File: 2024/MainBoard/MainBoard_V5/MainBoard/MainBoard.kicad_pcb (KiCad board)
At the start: 2 copper layers, 115.8 x 60.5 mm, 90 parts, among them J1 Raspberry_Pi_2_3, J11 ADC2, J12 ADC2, J13 Drib, J14 UART, J15 TFT3, J16 CAN_CON, J2 fan, J3 USB_C_Receptacle_USB2.0_16P, J4 Conn_01x02_Pin, J5 MOLEX MINISPOX, J6 Debug, J7 ADC0, Q1 NMOS, Q2 PMOS, Q3 PMOS, SW1 SW_MEC_5E, SW2 Ras_1, SW3 Ras_2, SW4 SW_Wuerth_450301014042, U1 STM32F446RETx, U2 CH340E, U3 MOUDLE-SEEEDUINO-XIAO, U7 AZ1117-3.3, U8 MAX3051, Y1 CSTNE16M0V530000R0

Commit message: 途中経過（配置、電源線）
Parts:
- removed D12: 1N4148, Diode_SMD:D_SOD-123
- removed D9: LED, LED_SMD:LED_0603_1608Metric_Pad1.05x0.95mm_HandSolder
- removed H3, H6: MountingHole_Pad, MountingHole:MountingHole_3.2mm_M3_Pad_Via
- removed J11, J12: ADC2, Connector_JST:JST_PH_S3B-PH-K_1x03_P2.00mm_Horizontal
- removed J5: MOLEX MINISPOX, Connector_Molex:Molex_SPOX_5268-06A_1x06_P2.50mm_Horizontal
- removed J7: ADC0, Connector_JST:JST_PH_S3B-PH-K_1x03_P2.00mm_Horizontal
- removed Q3: PMOS, Package_TO_SOT_SMD:SOT-23
- removed R14: 1k, Resistor_SMD:R_0603_1608Metric_Pad0.98x0.95mm_HandSolder
- removed R23: 10K, Resistor_SMD:R_0603_1608Metric_Pad0.98x0.95mm_HandSolder
- removed R8, R9: 2.2k, Resistor_SMD:R_0603_1608Metric_Pad0.98x0.95mm_HandSolder
- removed U6: ~, Connector_PinHeader_2.54mm:PinHeader_1x04_P2.54mm_Vertical
- added C19: 330u, Capacitor_SMD:CP_Elec_8x11.9, B.Cu at (-38.6, 27.7)
- added C20: 330u, Capacitor_SMD:CP_Elec_8x11.9, B.Cu at (-26.6, 27.7)
- added C21: 330u, Capacitor_SMD:CP_Elec_8x11.9, B.Cu at (8.30, -14.9)
- added C22: 1u, Capacitor_SMD:C_0603_1608Metric_Pad1.08x0.95mm_HandSolder, B.Cu at (-30.1, 12.6)
- added C23: 330u, Capacitor_SMD:CP_Elec_8x11.9, F.Cu at (58.4, 17.4)
- added C24: 330u, Capacitor_SMD:CP_Elec_8x11.9, B.Cu at (-59.4, -25.5)
- added C25: 330u, Capacitor_SMD:CP_Elec_8x11.9, F.Cu at (47.8, 22.5)
- added C26: 1u, Capacitor_SMD:C_0603_1608Metric_Pad1.08x0.95mm_HandSolder, B.Cu at (-45.3, 30.0)
- added C27: 330u, Capacitor_SMD:CP_Elec_8x11.9, F.Cu at (17.1, 23.9)
- added D15: LED, LED_SMD:LED_0603_1608Metric_Pad1.05x0.95mm_HandSolder, F.Cu at (58.6, -15.6)
- added D16: SR54F, Diode_SMD:D_SMB_Handsoldering, F.Cu at (10.3, 15.5)
- added J8: MOLEX MINISPOX, Connector_Molex:Molex_SPOX_5268-05A_1x05_P2.50mm_Horizontal, B.Cu at (0.55, 22.1)
- added PS1: P783F-Q24-S6-S, MainBoard:CONV_P783F-Q24-S6-S, F.Cu at (23.5, 28.7)
- added Q4: Q_PMOS_GDS, Package_TO_SOT_SMD:TO-252-2, F.Cu at (37.0, 16.6)
- added R17: 1k, Resistor_SMD:R_0603_1608Metric_Pad0.98x0.95mm_HandSolder, F.Cu at (58.6, -12.1)
- added R21: 10k, Resistor_SMD:R_0603_1608Metric_Pad0.98x0.95mm_HandSolder, F.Cu at (27.4, 10.9)
- added U10: MPU9250, Connector_PinHeader_2.54mm:PinHeader_1x10_P2.54mm_Vertical, F.Cu at (-6.41, -11.2)
- added U9: LM39300R-5.0, MainBoard:LM39300, B.Cu at (-35.8, 17.3)
- J4: value Conn_01x02_Pin -> metor
- Q1: value NMOS -> DMMT5401; footprint MainBoard:SOT95P240X111-3N -> Package_TO_SOT_SMD:SOT-23-6
- Q2: value PMOS -> Q_NMOS_GSD; footprint Package_TO_SOT_SMD:SOT-23 -> Package_TO_SOT_SMD:SOT-23-3
- R22, R7: value 1k -> 10k
- moved J13 98.0 mm to (50.8, -24.6), turned to 0 degrees
- moved C12 90.8 mm to (-45.5, 29.2), turned to 90 degrees
- moved J14 79.3 mm to (39.8, -24.6), turned to 0 degrees
- moved J6 60.7 mm to (19.7, -28.8)
- moved U3 49.6 mm to (-24.8, 12.0), turned to 180 degrees
- moved D4 48.2 mm to (2.90, 34.6)
- moved D5 48.2 mm to (0.40, 34.6)
- moved Q2 46.7 mm to (40.8, -16.5)
- moved LS1 37.7 mm to (25.0, -19.4)
- moved R7 37.5 mm to (27.7, -11.3)
- moved D6 26.5 mm to (12.0, 35.0)
- moved R10 26.5 mm to (12.3, 39.3)
- moved R11 26.5 mm to (10.3, 39.3)
- moved C18 25.0 mm to (35.6, 11.8), turned to 180 degrees
- moved R22 19.2 mm to (27.4, 12.5), turned to 0 degrees
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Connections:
- C14 pad 1: +5VL -> Net-(D16-K)
- C18 pad 1: +5V -> VBUS
- C18 pad 2: Net-(Q2-G) -> GND
- LS1 pad N: Net-(Q1-D) -> Net-(Q2-D)
- Q1 pad 1: Net-(Q1-D) -> Net-(Q1A-C1)
- Q1 pad 2: Net-(D4-K) -> Net-(Q1A-B1)
- Q1 pad 3: GND -> Net-(Q1A-B1)
- Q2 pad 1: Net-(Q2-D) -> Net-(D4-K)
- Q2 pad 2: Net-(Q2-G) -> GND
- Q2 pad 3: +5V -> Net-(Q2-D)
- R22 pad 1: Net-(Q2-G) -> Net-(Q1A-C1)
- R22 pad 2: +5V -> GND
- R7 pad 2: Net-(Q1-D) -> Net-(Q2-D)
- U1 pad 33: unconnected-(U1-PB12-Pad33) -> SPI2.CS
- U1 pad 34: unconnected-(U1-PB13-Pad34) -> SPI2.CLK
- U1 pad 35: unconnected-(U1-PB14-Pad35) -> SPI2.MISO
- U1 pad 36: unconnected-(U1-PB15-Pad36) -> SPI2.MOSI
- U1 pad 46: unconnected-(U1-PA13-Pad46) -> SWDIO
- U1 pad 50: SWDIO -> unconnected-(U1-PA15-Pad50)
- U1 pad 58: I2C_SCL -> unconnected-(U1-PB6-Pad58)
- U1 pad 59: I2C_SDA -> unconnected-(U1-PB7-Pad59)
- U7 pad 3: +5VL -> Net-(D16-K)
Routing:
- net GND: track 616.9 -> 181.4 mm, vias 260 -> 1
- net +3.3V: track 334.1 -> 181.7 mm, vias 2 -> 0
- net +6V: track 0.00 -> 119.3 mm
- net LED_CS: track 105.5 -> 0.00 mm
- net MISO: track 111.2 -> 7.12 mm, vias 2 -> 0
- net NRST: track 95.6 -> 0.00 mm, vias 3 -> 0
- net ADC_SUB0: track 95.2 -> 0.00 mm, vias 3 -> 0
- net ADC_PHOTO1: track 94.2 -> 0.00 mm, vias 4 -> 0
- net SCK: track 110.3 -> 20.8 mm, vias 2 -> 0
- net MOSI: track 115.1 -> 30.2 mm, vias 2 -> 0
- net ADC_PHOTO0: track 84.8 -> 0.00 mm, vias 3 -> 0
- net Ras_TX: track 82.0 -> 0.00 mm, vias 3 -> 0
- net UART1_RX: track 81.3 -> 0.00 mm, vias 4 -> 0
- net UART1_TX: track 79.9 -> 0.00 mm, vias 4 -> 0
- net Ras_RX: track 78.8 -> 0.00 mm, vias 1 -> 0
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- removed copper zone on B.Cu, net GND
- removed copper zone on F.Cu, net GND
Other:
- board size 115.8 x 60.5 mm -> 130.5 x 65 mm
- board text removed: "0"
- board text removed: "1"
- board text removed: "10k"
- board text removed: "120"
- board text removed: "1k"
- board text removed: "2"
- board text removed: "2.2k"
- board text removed: "3.3V"
- board text removed: "4.7k"
- board text removed: "5V"
- board text removed: "ADC"
- board text removed: "BNO055"
- board text removed: "C"
- board text removed: "CAN"
- board text removed: "CANH"
- board text removed: "CANL"
- board text removed: "Designed by Riku Miyazaki"
- board text removed: "Drib"
- board text removed: "GND"
- board text removed: "H"
- board text removed: "Mainboard v.4"
- board text removed: "NMOS"
- board text removed: "NRST"
- board text removed: "Osc"
- board text removed: "PMOS"
- board text removed: "Photo0"
- board text removed: "Power"
- board text removed: "R"
- board text removed: "RX"
- board text removed: "Ras1"
- board text removed: "Ras2"
- board text removed: "Ri-one"
- board text removed: "STM32 F446RE"
- board text removed: "SWCLK"
- board text removed: "SWDIO"
- board text removed: "Sound"
- board text removed: "TX"
- board text removed: "TypeC"
- board text removed: "USB← →SWD"
- board text removed: "VD"
- board text removed: "Write"
- board text removed: "X"
- board text removed: "Xiao RP2040"
- board text removed: "photo1"
- board text removed: "←1 2→"

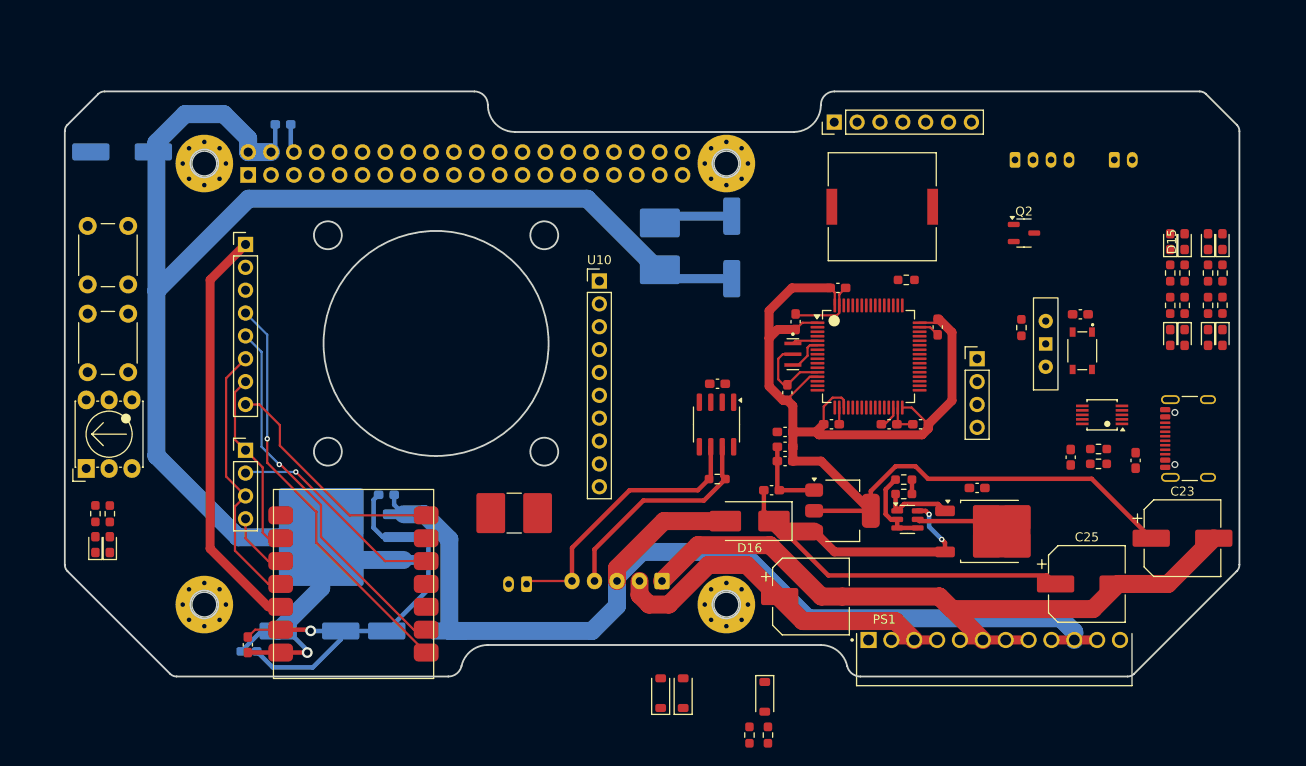
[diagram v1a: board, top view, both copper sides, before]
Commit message: アートワーク第一弾完成（ビア・シルク抜き）
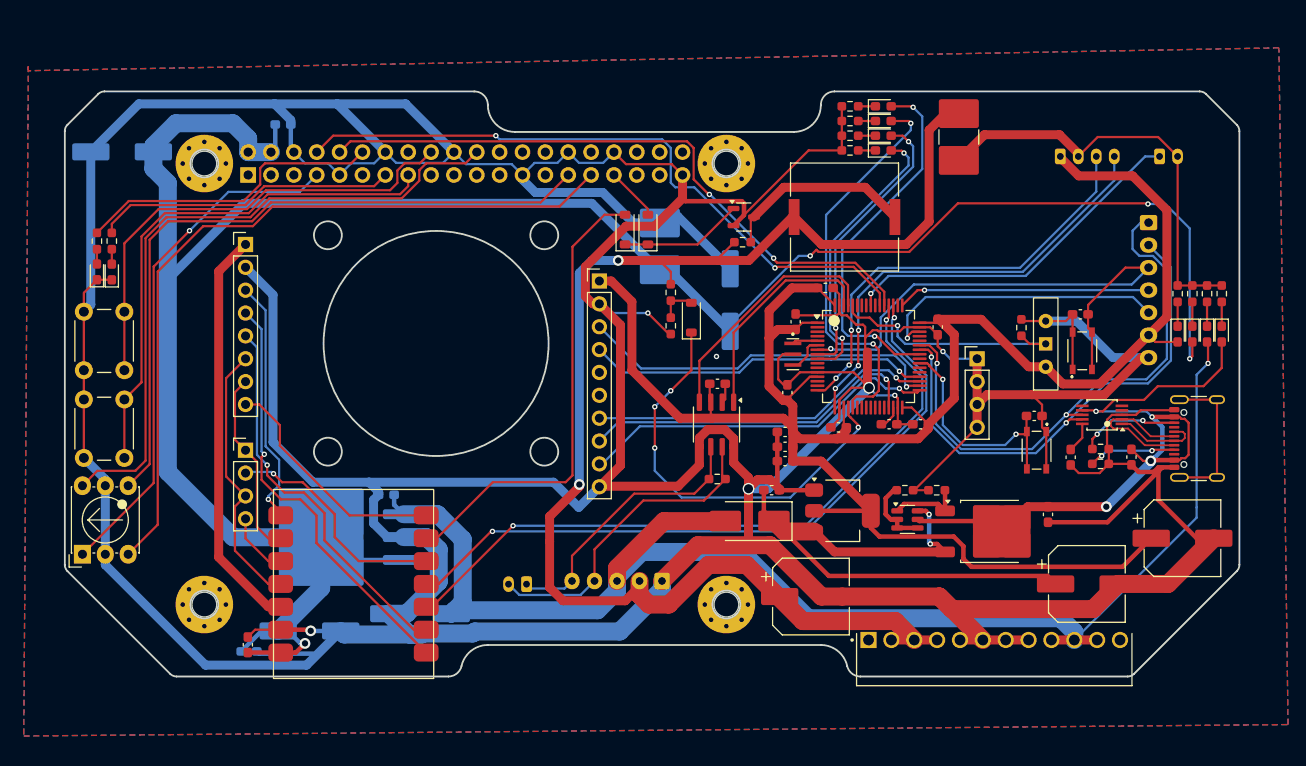
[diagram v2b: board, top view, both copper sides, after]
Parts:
- removed D2: LED, LED_SMD:LED_0603_1608Metric_Pad1.05x0.95mm_HandSolder
- removed R5: 1k, Resistor_SMD:R_0603_1608Metric_Pad0.98x0.95mm_HandSolder
- added C28: 0.1u, Capacitor_SMD:C_0603_1608Metric_Pad1.08x0.95mm_HandSolder, F.Cu at (41.9, 3.81)
- added D9: LED, LED_SMD:LED_0603_1608Metric_Pad1.05x0.95mm_HandSolder, F.Cu at (25.1, -25.7)
- added R14: 1k, Resistor_SMD:R_0603_1608Metric_Pad0.98x0.95mm_HandSolder, F.Cu at (21.4, -25.7)
- added SW5: SW_MEC_5E, MainBoard:SW_SKRPACE010, F.Cu at (42.2, 7.62)
- J6: footprint Connector_PinHeader_2.54mm:PinHeader_1x07_P2.54mm_Vertical -> Connector_JST:JST_XH_S7B-XH-A_1x07_P2.50mm_Horizontal; moved to B.Cu
- moved J4 64.7 mm to (33.5, -27.2), turned to 90 degrees
- moved D4 51.9 mm to (-3.56, -16.9)
- moved D5 51.5 mm to (-1.02, -16.9)
- moved R10 50.3 mm to (1.52, -9.91), turned to -90 degrees
- moved R11 46.3 mm to (1.52, -6.20)
- moved R15 43.3 mm to (21.4, -30.6), turned to 180 degrees
- moved D6 42.9 mm to (3.81, -7.11), turned to 90 degrees
- moved D10 42.2 mm to (25.1, -30.6), turned to 0 degrees
- moved R12 41.1 mm to (21.4, -29.0), turned to 180 degrees
- moved D7 39.9 mm to (25.1, -29.0), turned to 0 degrees
- moved R13 38.7 mm to (21.4, -27.3), turned to 180 degrees
- moved J6 36.7 mm to (54.6, -17.7), turned to -90 degrees
- moved D8 34.0 mm to (25.1, -27.3), turned to 0 degrees
- moved Q2 31.2 mm to (9.63, -18.3)
- moved D14 30.3 mm to (-60.6, -12.2)
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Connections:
- U1 pad 29: unconnected-(U1-PB10-Pad29) -> SPI2.INT
- U1 pad 39: unconnected-(U1-PC8-Pad39) -> imu.reset
- U10 pad 8: unconnected-(U10-INT-Pad8) -> SPI2.INT
- U2 pad 6: Net-(D2-A) -> unconnected-(U2-TNOW-Pad6)
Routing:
- net GND: track 181.4 -> 844.0 mm, vias 1 -> 7
- net VD: track 42.9 -> 154.9 mm, vias 0 -> 2
- net +3.3V: track 181.7 -> 275.7 mm
- net R3: track 0.00 -> 85.4 mm
- net R2: track 0.00 -> 77.8 mm
- net UART4_RX: track 0.00 -> 77.5 mm, vias 0 -> 2
- net UART4_TX: track 0.00 -> 77.0 mm, vias 0 -> 2
- net Ras_TX: track 0.00 -> 74.3 mm, vias 0 -> 2
- net R4: track 0.00 -> 74.3 mm
- net +5V: track 187.3 -> 261.4 mm, vias 1 -> 4
- net Ras_RX: track 0.00 -> 71.6 mm, vias 0 -> 2
- net VBUS: track 7.90 -> 73.4 mm, vias 0 -> 4
- net UART1_RX: track 0.00 -> 61.8 mm, vias 0 -> 2
- net SW_RAS2: track 0.00 -> 58.6 mm
- net NRST: track 0.00 -> 58.3 mm, vias 0 -> 1
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- added copper zone on B.Cu, net GND
- added copper zone on F.Cu, net GND

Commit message: 完成！！
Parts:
- added G***: LOGO, MainBoard:rionessl, B.Cu at (17.0, 10.0)
- added R8: 2.2k, Resistor_SMD:R_0603_1608Metric_Pad0.98x0.95mm_HandSolder, B.Cu at (2.08, -2.77)
- added R9: 2.2k, Resistor_SMD:R_0603_1608Metric_Pad0.98x0.95mm_HandSolder, B.Cu at (2.08, -1.17)
- added U6: BNO055, Connector_PinHeader_2.54mm:PinHeader_1x04_P2.54mm_Vertical, F.Cu at (-2.69, -3.71)
- J4: footprint Resistor_SMD:R_2816_7142Metric_Pad3.20x4.45mm_HandSolder -> Resistor_SMD:R_MiniMELF_MMA-0204
- Q4: footprint Package_TO_SOT_SMD:TO-252-2 -> Package_TO_SOT_SMD:SOT-23
- moved C28 25.3 mm to (47.0, -20.9), turned to 0 degrees
- moved SW5 25.2 mm to (47.2, -17.1), turned to 90 degrees
- moved R1 12.3 mm to (40.7, -18.3), turned to 0 degrees
- moved SW4 7.77 mm to (42.5, -11.9)
- moved SW1 2.07 mm to (47.2, -5.50)
- moved C9 2.07 mm to (47.0, -9.55)
- moved Q4 1.83 mm to (35.6, 15.5)
- moved C22 1.27 mm to (-28.8, 12.6)
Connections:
- U1 pad 58: unconnected-(U1-PB6-Pad58) -> I2C_SCL
- U1 pad 59: unconnected-(U1-PB7-Pad59) -> I2C_SDA
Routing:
- net I2C_SCL: track 0.00 -> 36.7 mm, vias 0 -> 1
- net I2C_SDA: track 0.00 -> 34.1 mm, vias 0 -> 1
- net +3.3V: track 275.7 -> 301.4 mm
- net imu.reset: track 25.2 -> 38.2 mm
- net GND: track 844.0 -> 837.0 mm, vias 7 -> 115
- net Net-(SW4-B): track 27.5 -> 32.3 mm, vias 1 -> 0
- net VBUS: track 73.4 -> 77.5 mm
- net Net-(D16-K): track 65.6 -> 68.7 mm
- net Net-(Q1A-C1): track 8.25 -> 11.2 mm
- net Reset: track 47.6 -> 49.9 mm
- net SWDIO: track 32.7 -> 30.6 mm
- net LED0: track 44.8 -> 42.8 mm
- net +5V: track 261.4 -> 263.0 mm
- net T_CS: track 25.7 -> 24.2 mm
- net D/C: track 43.0 -> 44.3 mm
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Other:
- board text added: "0"
- board text added: "0.1"
- board text added: "0.1u"
- board text added: "1"
- board text added: "10k"
- board text added: "120"
- board text added: "1k"
- board text added: "1u"
- board text added: "2"
- board text added: "2.2k"
- board text added: "2024"
- board text added: "3.3V"
- board text added: "4.7k"
- board text added: "4.7u"
- board text added: "5.1k"
- board text added: "5V"
- board text added: "6.5V"
- board text added: "BNO055"
- board text added: "CAN"
- board text added: "CANH"
- board text added: "CANL"
- board text added: "CLK"
- board text added: "DIO"
- board text added: "Designed by Riku Miyazaki"
- board text added: "Dip"
- board text added: "Drib"
- board text added: "Fan"
- board text added: "GND"
- board text added: "H"
- board text added: "MPU9250"
- board text added: "MainBoard v5"
- board text added: "NMOS"
- board text added: "OSC"
- board text added: "PMOS"
- board text added: "PNP+PNP"
- board text added: "Power"
- board text added: "R"
- board text added: "RST"
- board text added: "RX"
- board text added: "Ras"
- board text added: "Ras1"
- board text added: "Ras2"
- board text added: "Ri-one"
- board text added: "Riku"
- board text added: "STM32 F446RE"
- board text added: "Sound"
- board text added: "Switch 1"
- board text added: "Switch 2"
- board text added: "TX"
- board text added: "TypeC"
- board text added: "VD"
- board text added: "Xiao RP2040"

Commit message: 最終版
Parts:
- moved R1 1.91 mm to (40.7, -20.2)
- moved C9 0.75 mm to (47.0, -8.80)
- moved SW1 0.63 mm to (47.2, -4.88)
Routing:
- net GND: track 837.0 -> 838.9 mm
- net Net-(SW4-B): track 32.3 -> 34.2 mm
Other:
- board text added: "IMU"
- board text added: "Reset"
- board text added: "USB← →SWD"
